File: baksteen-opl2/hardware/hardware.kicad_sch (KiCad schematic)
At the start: 25 parts

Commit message: ...
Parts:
- removed D? (x5): Blue, LED_THT:LED_D3.0mm_IRBlack, symbol LED:IR204A
- removed D?: (no value), symbol LED:IR204A
- removed R? (x5): 1k, symbol Device:R
- removed R?: (no value), symbol Device:R
- removed U?: (no value), symbol 74xx:74HC595
- added D? (x8): WS2812, LED_SMD:LED_WS2812_PLCC6_5.0x5.0mm_P1.6mm, symbol LED:WS2812
- added D?: (no value), symbol LED:WS2812
- A?: value (none) -> Nano v3.x; footprint (none) -> Module:Arduino_Nano
- J?: value (none) -> OPL
- R?: value (none) -> 10k
- SW?: value (none) -> Encoder
- U?: value (none) -> 74HC165
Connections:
- net 5V: now also D?.3 (VCC), D?.3 (VCC), D?.3 (VCC), D?.3 (VCC), D?.3 (VCC), D?.3 (VCC), D?.3 (VCC), D?.3 (VCC), D?.3 (VCC), D?.5 (VDD), D?.5 (VDD), D?.5 (VDD), D?.5 (VDD), D?.5 (VDD), D?.5 (VDD), D?.5 (VDD), D?.5 (VDD), D?.5 (VDD)
- net GND: now also D?.6 (VSS), D?.6 (VSS), D?.6 (VSS), D?.6 (VSS), D?.6 (VSS), D?.6 (VSS), D?.6 (VSS), D?.6 (VSS), D?.6 (VSS)
- net PIXELS: now reaches A?.2 (D0/RX)
- net PIXELS: now also D?.2 (DIN)
- net SHIFT_DATA renamed SHIFT_DATAOUT
- new net: D?.1 (DOUT), D?.2 (DIN) (x8)

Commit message: added power symbols, and NC to schematic
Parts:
- removed D?: WS2812, LED_SMD:LED_WS2812_PLCC6_5.0x5.0mm_P1.6mm, symbol LED:WS2812
- removed J?: OPL, symbol Connector_Generic_MountingPin:Conn_01x07_MountingPin
- added J1: (no value), symbol Connector_Generic:Conn_01x07
- added J10, J2, J3, J4, J5, J6, J7, J9: AudioJack2, symbol Connector:AudioJack2
- added J11: (no value), symbol Connector_Generic:Conn_02x05_Odd_Even
- added J8: (no value), symbol Connector:AudioJack2
- added U2: (no value), symbol Regulator_Linear:LM7805_TO220
- gave numbers to parts that had none: 19
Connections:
- net 5V is gone; now on net +5V: A1.27 (+5V), D1.3 (VCC), D1.5 (VDD), D2.3 (VCC), D2.5 (VDD), D3.3 (VCC), D3.5 (VDD), D4.3 (VCC), D4.5 (VDD), D5.3 (VCC), D5.5 (VDD), D6.3 (VCC), D6.5 (VDD), D7.3 (VCC), D7.5 (VDD), D8.3 (VCC), D8.5 (VDD), U1.16 (VCC)
- net A0: now also J1.3 (Pin_3)
- net CV1: now also J9.T
- net CV2: now also J10.T
- net DATA: now also J1.4 (Pin_4)
- net GATE1: now also J2.T
- net GATE2: now also J3.T
- net GATE3: now also J4.T
- net GATE4: now also J5.T
- net GATE5: now also J6.T
- net GATE6: now also J7.T
- net GND: now also A1.22 (A3), A1.23 (A4), A1.24 (A5), A1.25 (A6), A1.26 (A7), J1.2 (Pin_2), J10.S, J11.3 (Pin_3), J11.4 (Pin_4), J11.5 (Pin_5), J11.6 (Pin_6), J11.7 (Pin_7), J11.8 (Pin_8), J2.S, J3.S, J4.S, J5.S, J6.S, J7.S, J8.S, J9.S, U2.2 (GND)
- net LATCH: now also J1.5 (Pin_5)
- net RESET: now also J1.7 (Pin_7)
- net SHIFT: now also J1.6 (Pin_6)
- net V/OCT: now also J8.T
- net +5V: now reaches A1.18 (AREF)
- net +5V: now also J1.1 (Pin_1), U2.3 (VO)
- new net +12V: J11.10 (Pin_10), J11.9 (Pin_9), U2.1 (VI)
- new net -12V: J11.1 (Pin_1), J11.2 (Pin_2)
- no-connect marks 0 -> 6
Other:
- moved on the sheet: D1, D2, D3, D4, D5, D6, D7, D8

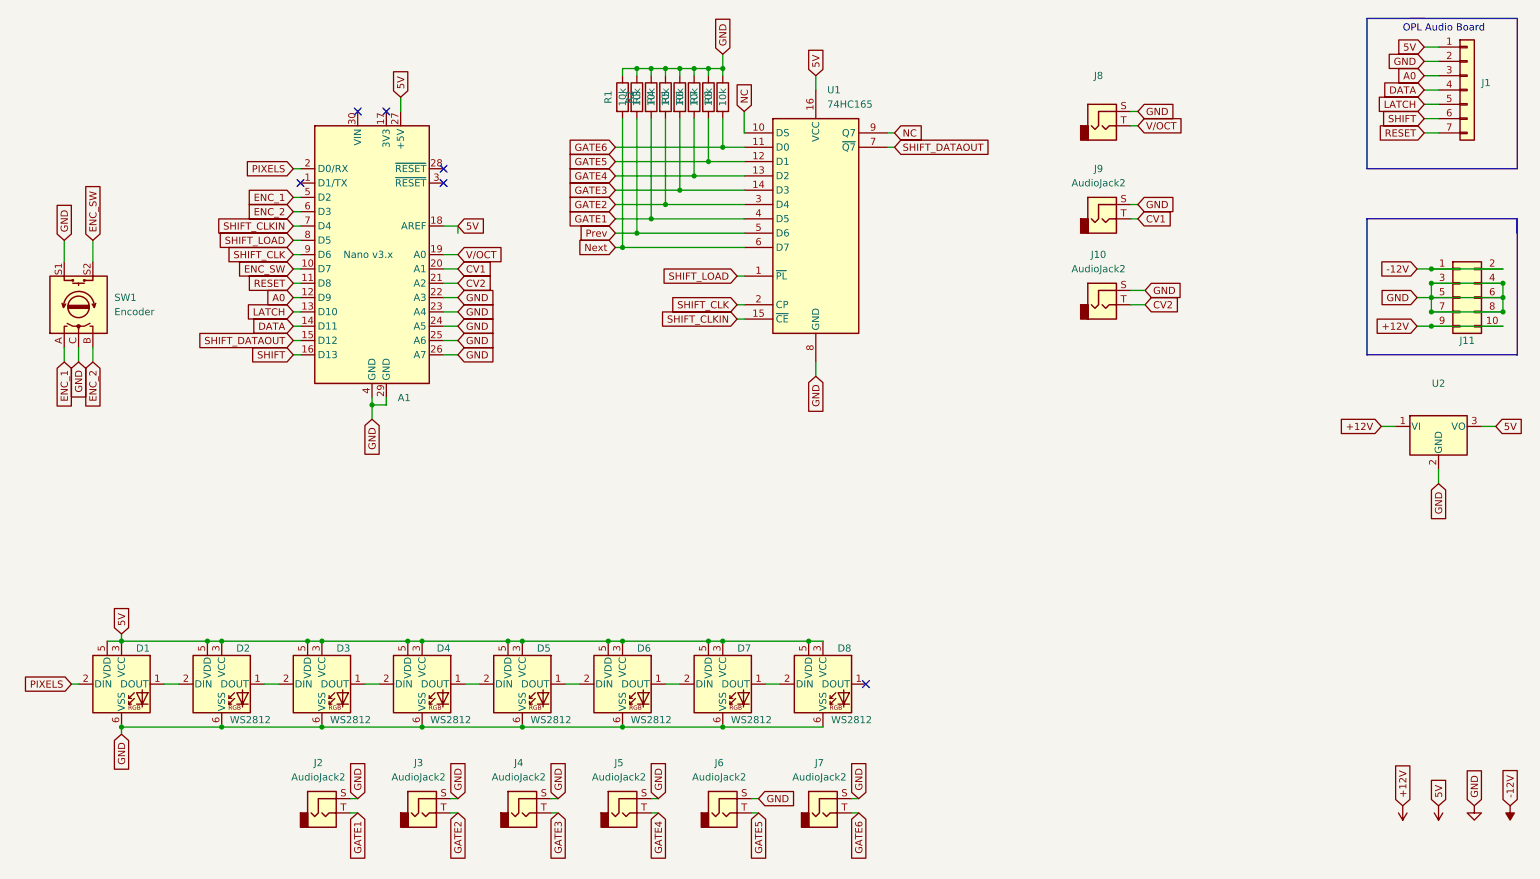
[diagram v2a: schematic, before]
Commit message: updated schematic to include CV components, laid out components on PCB ... no traces run yet
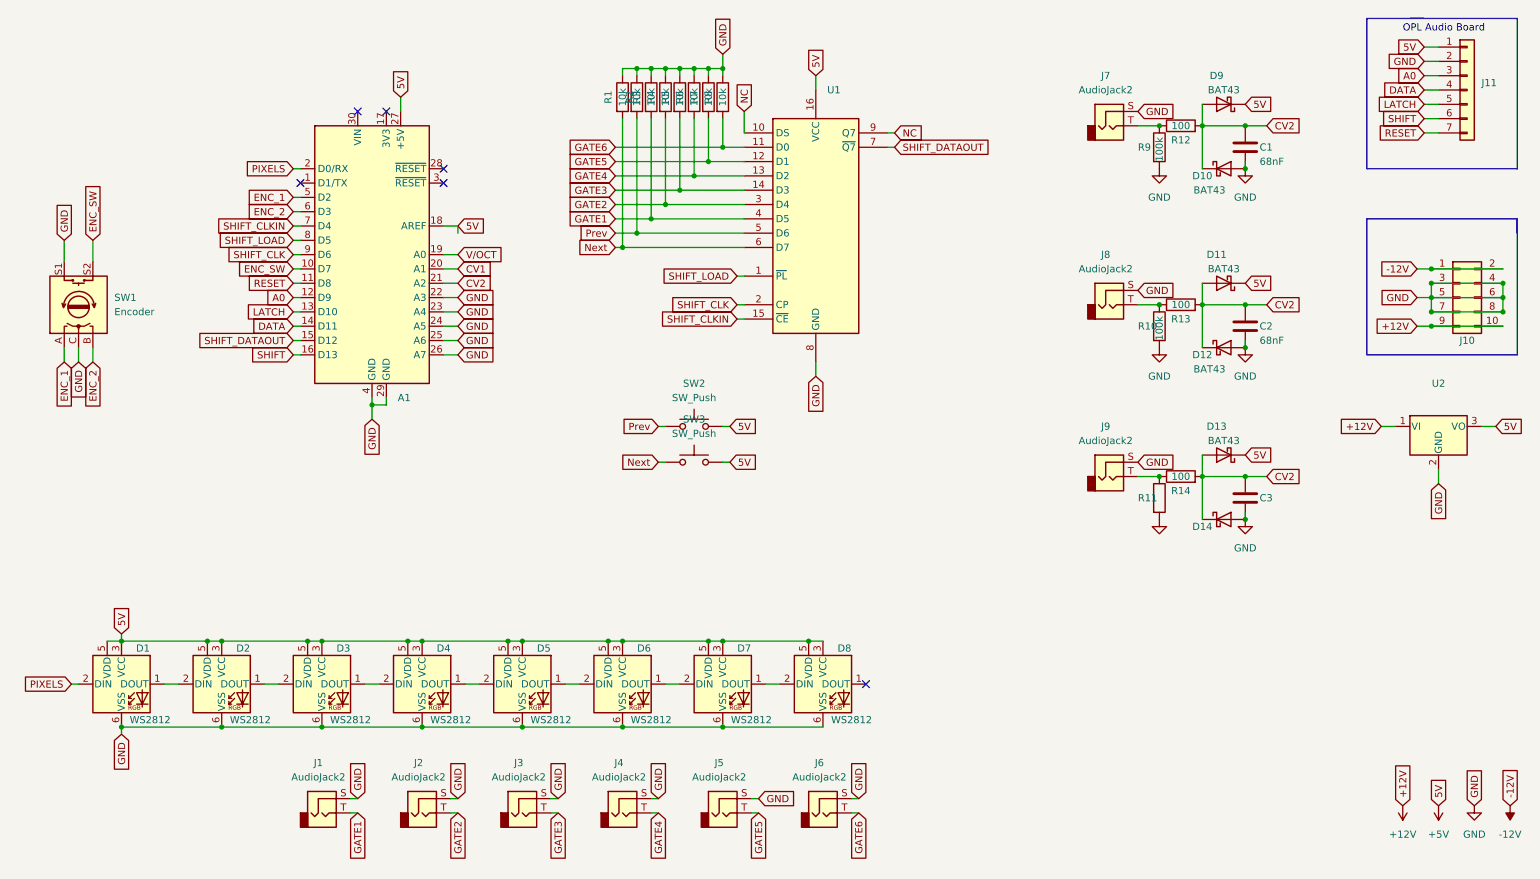
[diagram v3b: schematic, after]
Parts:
- added C1, C2: 68nF, symbol Device:C
- added C3: (no value), symbol Device:C
- added D10, D11, D12, D13, D9: BAT43, symbol Diode:BAT43
- added D14: (no value), symbol Diode:BAT43
- added R10, R9: 100k, symbol Device:R
- added R11: (no value), symbol Device:R
- added R12, R13, R14: 100, symbol Device:R
- added SW2, SW3: SW_Push, Button_Switch_THT:SW_PUSH_6mm_H5mm, symbol Switch:SW_Push
- A1: value Nano v3.x -> (none); footprint Module:Arduino_Nano -> (none)
- D1: value (none) -> WS2812; footprint (none) -> LED_SMD:LED_WS2812_PLCC6_5.0x5.0mm_P1.6mm
- J1: renamed from J2; footprint (none) -> Connector_Audio:Jack_3.5mm_QingPu_WQP-PJ398SM_Vertical_CircularHoles
- J2: renamed from J3; footprint (none) -> Connector_Audio:Jack_3.5mm_QingPu_WQP-PJ398SM_Vertical_CircularHoles
- J3: renamed from J4; footprint (none) -> Connector_Audio:Jack_3.5mm_QingPu_WQP-PJ398SM_Vertical_CircularHoles
- J4: renamed from J5; footprint (none) -> Connector_Audio:Jack_3.5mm_QingPu_WQP-PJ398SM_Vertical_CircularHoles
- J5: renamed from J6; footprint (none) -> Connector_Audio:Jack_3.5mm_QingPu_WQP-PJ398SM_Vertical_CircularHoles
- J6: renamed from J7; footprint (none) -> Connector_Audio:Jack_3.5mm_QingPu_WQP-PJ398SM_Vertical_CircularHoles
- J7: renamed from J8; value (none) -> AudioJack2; footprint (none) -> Connector_Audio:Jack_3.5mm_QingPu_WQP-PJ398SM_Vertical_CircularHoles
- J8: renamed from J9; footprint (none) -> Connector_Audio:Jack_3.5mm_QingPu_WQP-PJ398SM_Vertical_CircularHoles
- J9: renamed from J10; footprint (none) -> Connector_Audio:Jack_3.5mm_QingPu_WQP-PJ398SM_Vertical_CircularHoles
- SW1: footprint (none) -> Rotary_Encoder:RotaryEncoder_Alps_EC11E-Switch_Vertical_H20mm
- U1: value 74HC165 -> (none)
- renumbered J11 to J10, J1 to J11
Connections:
- net +5V: now also D11.1 (K), D13.1 (K), D9.1 (K), SW2.2, SW3.2
- net CV1: no longer J8.T
- net CV2: now also C1.1, C2.1, C3.1, D10.1 (K), D11.2 (A), D12.1 (K), D13.2 (A), D14.1 (K), D9.2 (A), R12.2, R13.2, R14.2; no longer J9.T
- net GND: now also C1.2, C2.2, C3.2, D10.2 (A), D12.2 (A), D14.2 (A), R10.2, R11.2, R9.2
- net Next: now also SW3.1
- net Prev: now also SW2.1
- net V/OCT: no longer J7.T
- new net: J9.T, R11.1, R14.1
- new net: J8.T, R10.1, R13.1
- new net: J7.T, R12.1, R9.1
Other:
- moved on the sheet: J7, J8, J9
